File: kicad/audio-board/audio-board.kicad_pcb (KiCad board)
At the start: 4 copper layers, 70 x 50 mm, 120 parts, among them J1 AERONODE_FFC (mates J9), J3 CUP_L (A2B + speaker), J4 CUP_R (speaker), J5 PANEL (ear + mic), J6 FAILSAFE_ELECTRET, Q1 AO3401A, Q2 2N7002, T2 Triad SP-74 (cup L), T3 Triad SP-74 (cup R), T4 Bourns SM-LP-5001 (600:600), U1 TPS62162DSG, U10 AQW612S (K1 mic-hi), U11 AQW612S (K1 mic-lo), U12 LM2731XMF (8 V A2B bus), U2 TPS62160DSG, U3 ADP7118AUJZ-3.3-R7, U4 ADAU1467, U5 W25Q32JVSS, U6 ADAU1372, U7 IM68A130A, U9 AD2428WBCPZ, Y1 SiT8008 12.288MHz 3.3V

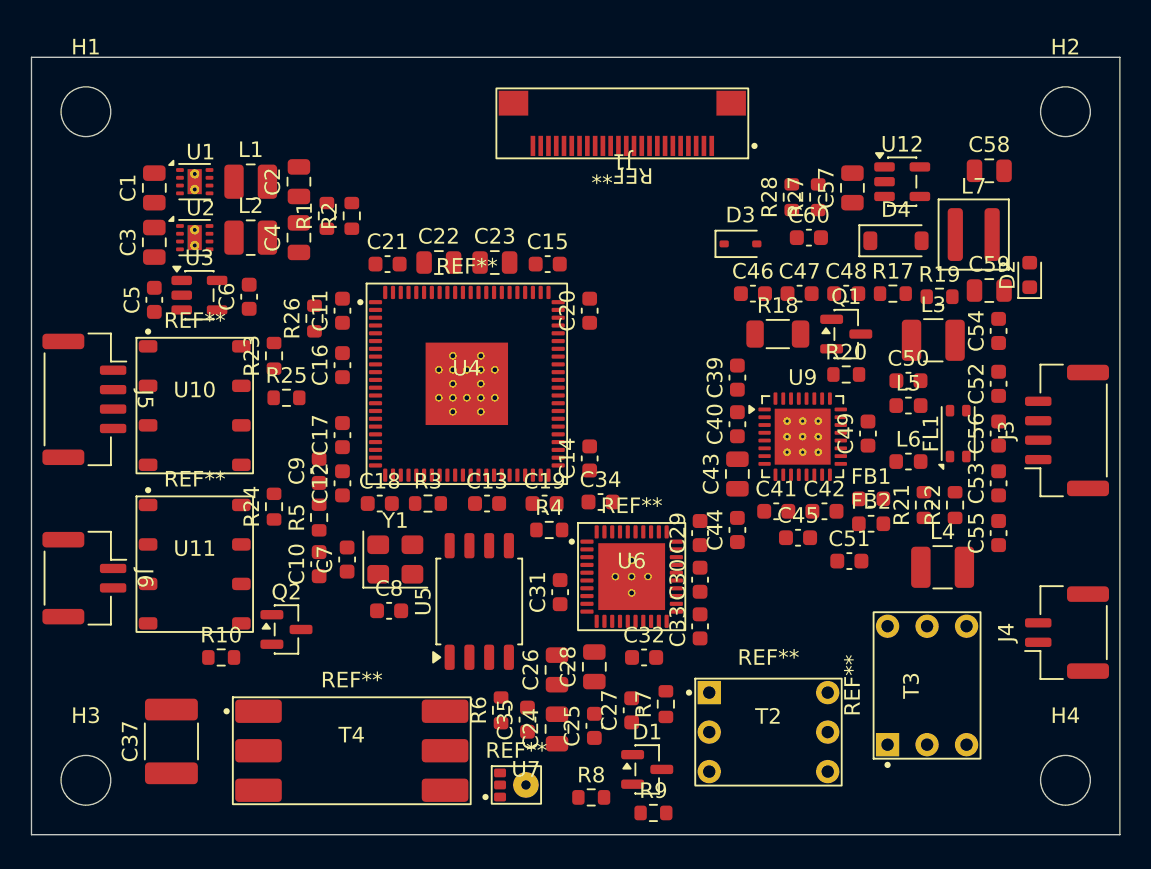
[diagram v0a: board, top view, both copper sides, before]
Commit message: [LIMA] audio PCB: GND/+3V3 plane fanout (126 pad vias + 21 EP vias), DRC 0
Scripted (doc/route/fanout.py, pcbnew, KiCad closed) - last autoroute stalled on plane fanout.

Co-Authored-By: Claude Opus 5.5 <noreply@anthropic.com>
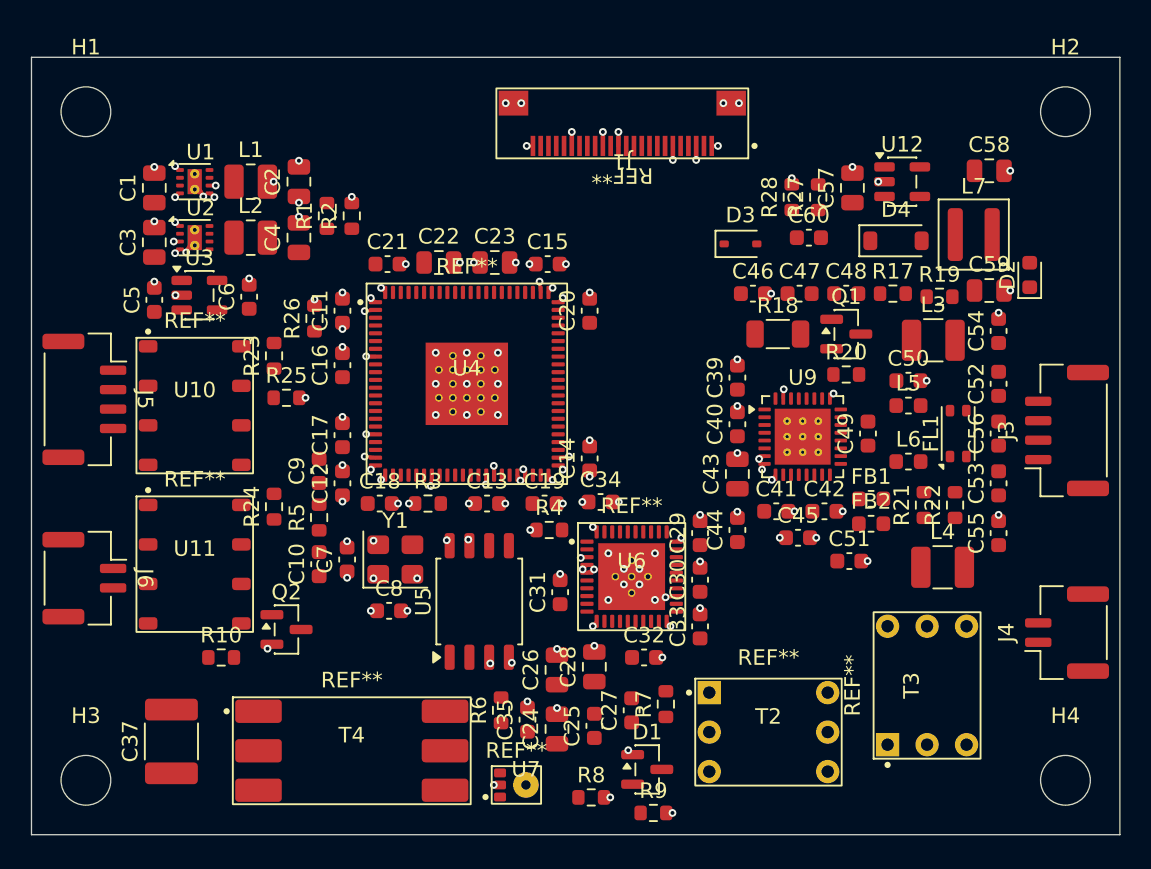
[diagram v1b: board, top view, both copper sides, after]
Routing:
- net /GND: track 0.00 -> 44.9 mm, vias 0 -> 119
- net /+3V3: track 0.00 -> 12.3 mm, vias 0 -> 28

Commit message: [LIMA] audio PCB: Freerouting pass (WIP) - 19 pads unconnected, 0 clearance errors
In1 GND / In2 +3V3 planes kept solid; VBAT/+3V3A routed 0.2 mm (fine-pitch pins), other power 0.3 mm.
Left: A2B I2S lines U4<->U9, some +3V3A/A2B_VIN links, 5 neckdowns <0.127 mm.

Co-Authored-By: Claude Opus 5.5 <noreply@anthropic.com>
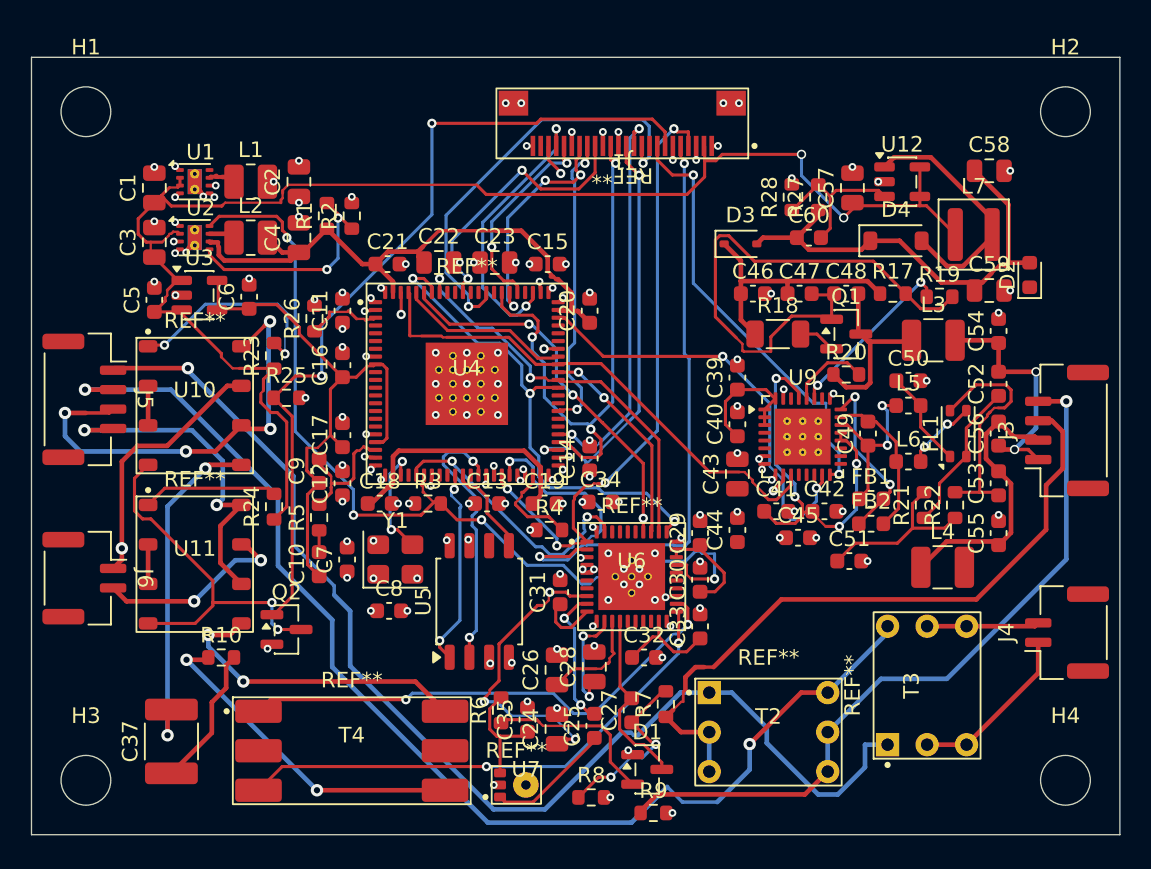
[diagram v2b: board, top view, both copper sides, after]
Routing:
- net /VBAT: track 0.00 -> 96.8 mm, vias 0 -> 2
- net /EAR_RTN: track 0.00 -> 76.6 mm, vias 0 -> 2
- net /EAR_HI: track 0.00 -> 75.5 mm, vias 0 -> 1
- net /RESET_N: track 0.00 -> 60.4 mm, vias 0 -> 4
- net /+3V3A: track 0.00 -> 58.9 mm
- net /+1V2: track 0.00 -> 54.8 mm
- net /CTL_MIC: track 0.00 -> 54.3 mm, vias 0 -> 2
- net /I2C_SCL: track 0.00 -> 50.6 mm, vias 0 -> 3
- net /SPK_L_B: track 0.00 -> 47.7 mm, vias 0 -> 1
- net /SPK_L_A: track 0.00 -> 44.6 mm
- net /I2C_SDA: track 0.00 -> 40.2 mm, vias 0 -> 4
- net /I2S_BCLK: track 0.00 -> 36.9 mm, vias 0 -> 3
- net /A2B_GATE: track 0.00 -> 35.8 mm
- net /DAC_N: track 0.00 -> 33.4 mm, vias 0 -> 2
- net /A2B_SYNC: track 0.00 -> 32.9 mm
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
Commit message: [LIMA] audio PCB: placement rev2 - boost cell tightened, U9 rotated to face hub (unrouted)
Back to the unrouted 3ab5285 board. L7 turned 180 so SW pad meets D4 anode; U12 r180 above L7
(SW node pads now ~2-3 mm apart, was 16 mm routed); C57/C59 at U12 VBAT / D4 cathode.
U9 r-90, 2 mm left: TDM pins 9-16 face U4; its 7 decaps re-placed at their pins; FB1/FB2 +0.4 mm.
DRC 0 violations. T2/T3 not moved (pending Peter: moving them lengthens 4 SPK nets).
Routed WIP stays in history at c929354.

Co-Authored-By: Claude Opus 5.5 <noreply@anthropic.com>
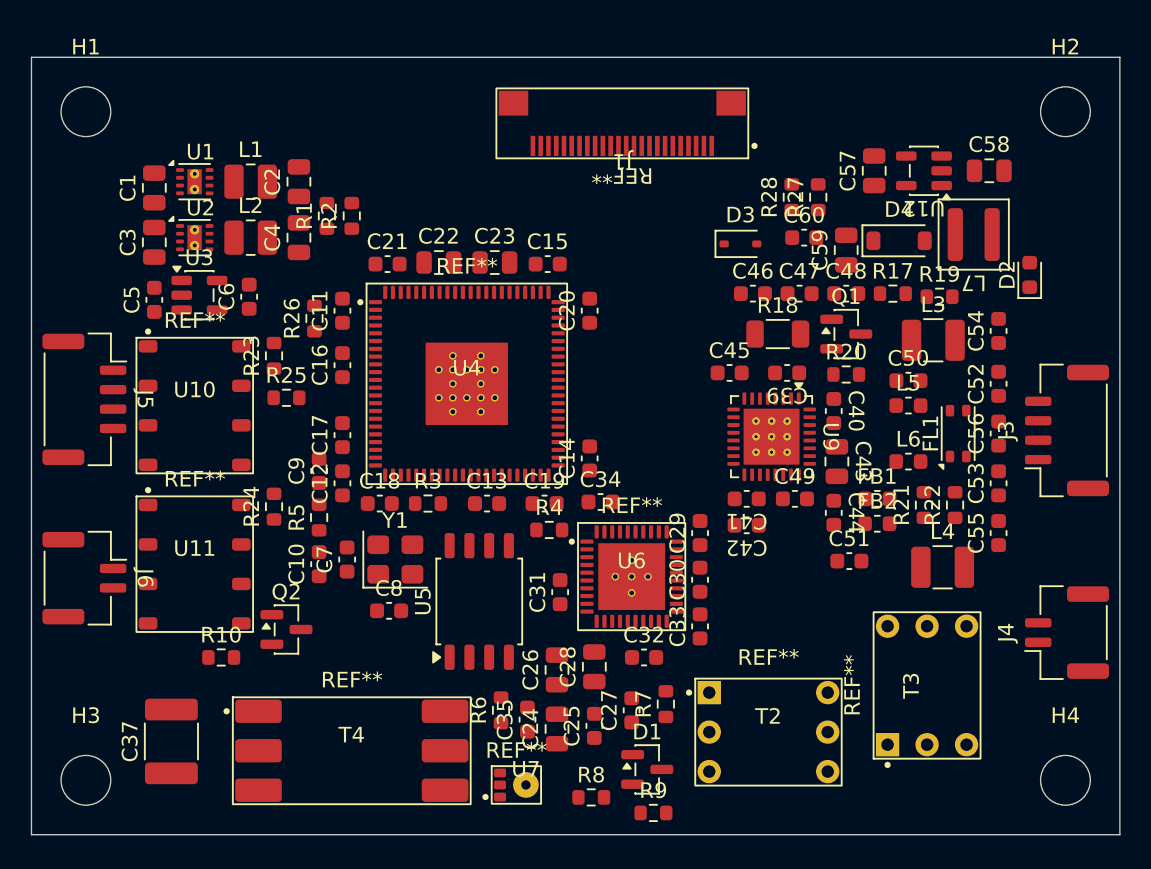
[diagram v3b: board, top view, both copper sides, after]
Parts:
- moved C45 11.5 mm to (144.9, 100.3)
- moved C59 9.56 mm to (152.4, 92.4), turned to 90 degrees
- moved C43 6.45 mm to (151.8, 106.0), turned to -90 degrees
- moved C49 6.30 mm to (149.1, 108.4), turned to 0 degrees
- moved C44 6.30 mm to (151.6, 109.3), turned to -90 degrees
- moved C40 6.26 mm to (151.6, 102.8), turned to -90 degrees
- moved C42 5.08 mm to (146.0, 110.1), turned to 180 degrees
- moved C39 3.21 mm to (148.6, 100.3), turned to 180 degrees
- moved C41 2.06 mm to (146.0, 108.4), turned to 180 degrees
- moved U9 2.00 mm to (147.6, 104.4), turned to -90 degrees
- moved C57 1.78 mm to (154.2, 87.3)
- moved U12 1.57 mm to (157.4, 87.3), turned to 180 degrees
- moved FB1 0.40 mm to (154.4, 108.4)
- moved FB2 0.40 mm to (154.4, 110.0)
- moved C60 0.30 mm to (149.7, 91.6)
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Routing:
- net /VBAT: track 96.8 -> 0.00 mm, vias 2 -> 0
- net /EAR_RTN: track 76.6 -> 0.00 mm, vias 2 -> 0
- net /EAR_HI: track 75.5 -> 0.00 mm, vias 1 -> 0
- net /RESET_N: track 60.4 -> 0.00 mm, vias 4 -> 0
- net /+3V3A: track 58.9 -> 0.00 mm
- net /+1V2: track 54.8 -> 0.00 mm
- net /CTL_MIC: track 54.3 -> 0.00 mm, vias 2 -> 0
- net /I2C_SCL: track 50.6 -> 0.00 mm, vias 3 -> 0
- net /SPK_L_B: track 47.7 -> 0.00 mm, vias 1 -> 0
- net /GND: track 44.9 -> 0.00 mm, vias 119 -> 0
- net /SPK_L_A: track 44.6 -> 0.00 mm
- net /I2C_SDA: track 40.2 -> 0.00 mm, vias 4 -> 0
- net /I2S_BCLK: track 36.9 -> 0.00 mm, vias 3 -> 0
- net /A2B_GATE: track 35.8 -> 0.00 mm
- net /DAC_N: track 33.4 -> 0.00 mm, vias 2 -> 0
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
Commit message: [LIMA] audio PCB: EAR corridor, isolation turns, hand routes, plane fanout (pre-autoroute)
- U10/U11/T4 turned 180: aircraft-side pins now face J5/J6 and the aircraft corner
  (U10 LED pins were 0.8 mm from J5's EAR pads); T4 DAC side now faces the codec.
- In1/In2 cut back under the EAR corridor, T2 and T3 (doc/route/planecut.py).
- Hand routes (locked, doc/route/hand-routes.json): EAR pair B.Cu bottom edge 0.3/0.55 gap,
  EAR_HI T2->T3 link on F.Cu; boost SW node 0.6/0.8 mm, D4->C59, C57->U12 VBAT; A2B LINE_P/N at J3.
- Plane fanout re-run, now aware of B.Cu tracks and the plane outline.
DRC: 0 violations, 196 unconnected (to autoroute).

Co-Authored-By: Claude Opus 5.5 <noreply@anthropic.com>
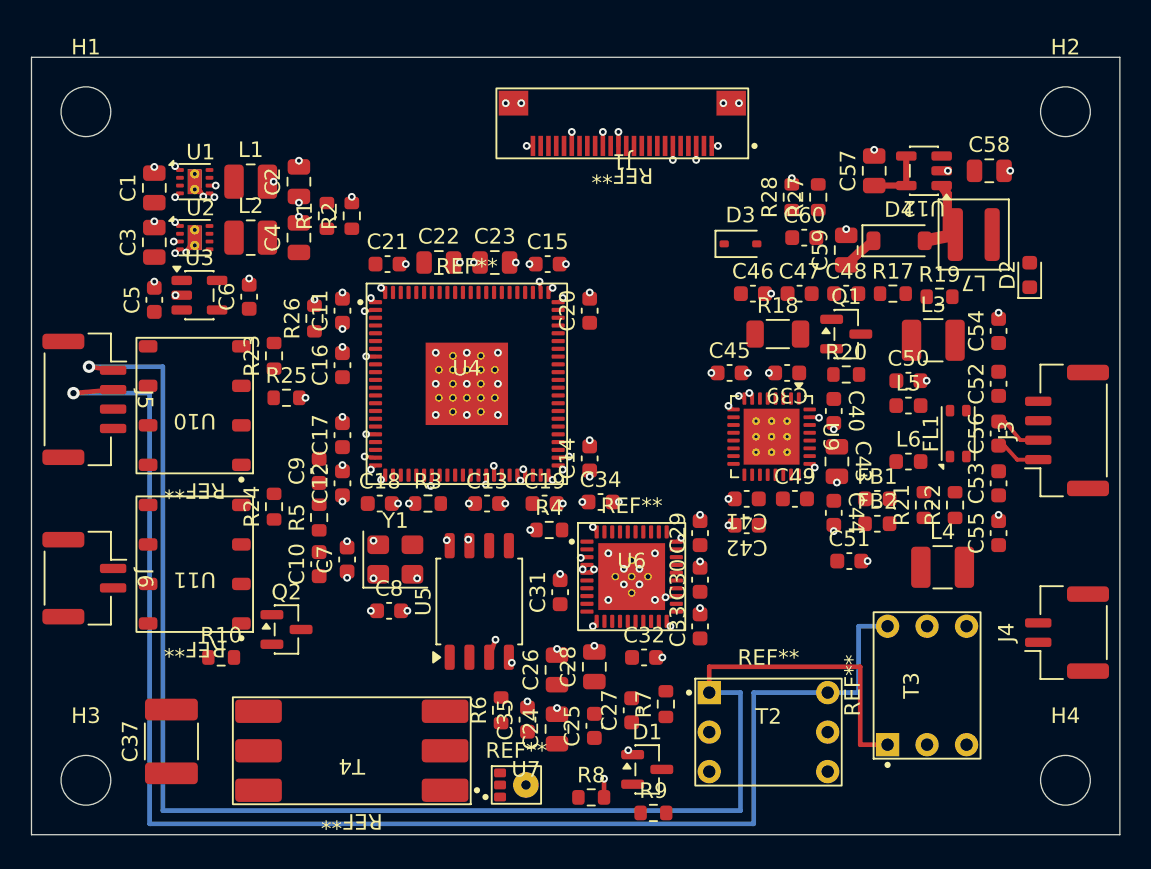
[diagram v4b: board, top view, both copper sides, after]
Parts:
- turned T4 to 180 degrees
- turned U10 to 180 degrees
- turned U11 to 180 degrees
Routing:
- net /EAR_HI: track 0.00 -> 99.8 mm, vias 0 -> 1
- net /EAR_RTN: track 0.00 -> 95.3 mm, vias 0 -> 1
- net /GND: track 0.00 -> 44.5 mm, vias 0 -> 116
- net /+3V3: track 0.00 -> 13.1 mm, vias 0 -> 28
- net /BOOST_SW: track 0.00 -> 5.77 mm
- net /VBAT: track 0.00 -> 3.96 mm
- net /A2B_LINE_N: track 0.00 -> 3.11 mm
- net /A2B_LINE_P: track 0.00 -> 2.94 mm
- net /VBUS8: track 0.00 -> 2.34 mm

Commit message: [LIMA] audio PCB: autoroute on the corridor build - 18 unconnected, 0 clearance errors (WIP)
Scripted pipeline doc/route/build.sh (rev2 placement -> isolation turns -> U9 cap column moved out
-> plane cut -> hand routes -> fanout -> DSN). Freerouting best variant: In2 kept a solid plane,
0.13 mm clearance, 0.5/0.25 vias. SES import + tolerant de-dupe (pcbnew segfault workarounds).

Co-Authored-By: Claude Opus 5.5 <noreply@anthropic.com>
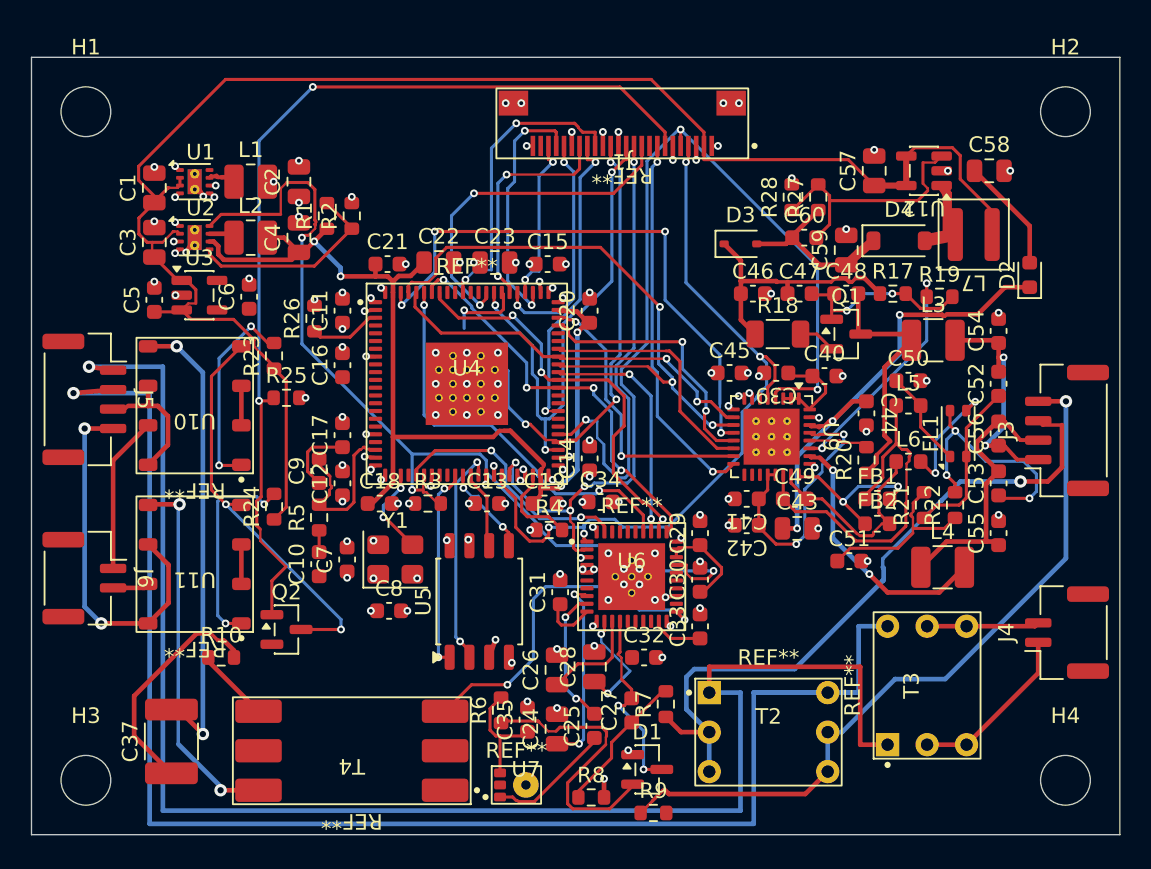
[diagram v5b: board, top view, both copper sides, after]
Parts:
- moved C44 6.74 mm to (153.7, 102.9)
- moved R20 5.65 mm to (153.7, 105.9), turned to 90 degrees
- moved C43 5.00 mm to (149.2, 110.3), turned to 0 degrees
- moved C40 2.33 mm to (151.0, 100.5), turned to 0 degrees
- moved C39 0.70 mm to (147.9, 100.3)
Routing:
- net /VBAT: track 3.96 -> 104.7 mm
- net /+1V2: track 0.00 -> 65.0 mm, vias 0 -> 4
- net /I2C_SCL: track 0.00 -> 64.7 mm, vias 0 -> 5
- net /CTL_MIC: track 0.00 -> 62.4 mm, vias 0 -> 2
- net /RESET_N: track 0.00 -> 61.8 mm, vias 0 -> 3
- net /I2C_SDA: track 0.00 -> 49.0 mm, vias 0 -> 4
- net /SPK_L_B: track 0.00 -> 47.7 mm, vias 0 -> 1
- net /SPK_L_A: track 0.00 -> 44.9 mm, vias 0 -> 1
- net /A2B_SYNC: track 0.00 -> 38.2 mm, vias 0 -> 3
- net /A2B_DTX0: track 0.00 -> 36.6 mm, vias 0 -> 4
- net /I2S_BCLK: track 0.00 -> 35.2 mm, vias 0 -> 4
- net /I2S_WS: track 0.00 -> 32.6 mm, vias 0 -> 3
- net /A2B_VIN: track 0.00 -> 31.0 mm, vias 0 -> 3
- net /PV_OUT: track 0.00 -> 30.2 mm, vias 0 -> 2
- net /HOST_SDI0: track 0.00 -> 29.8 mm, vias 0 -> 2
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
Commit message: [LIMA] audio PCB: fully routed - 0 unconnected, 0 DRC errors
Freerouting left 18; finished with doc/route/maze.py (A* on F.Cu/B.Cu over the real copper,
clearance-inflated) - 16/18 at 0.2 mm, then C33 moved +0.8 mm to open U6's DAC corner, DAC pair
ripped and re-routed with C33's links. Shadow duplicates from SES import removed.
Hand-check [measured]: BOOST_SW 5.8 mm (was 16); EAR_HI/RTN 99.8/95.3 mm, pair over no plane;
all EAR/MIC/ELEC/PV copper over no plane; SPK (isolated secondaries) cross planes.
DRC remaining: silk warnings, 116 lib_footprint_mismatch (known), 5 datasheet-field parity warnings.

Co-Authored-By: Claude Opus 5.5 <noreply@anthropic.com>
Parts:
- moved C33 0.80 mm to (143.8, 116.6)
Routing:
- net /+3V3A: track 29.5 -> 88.1 mm, vias 0 -> 12
- net /GND: track 44.5 -> 82.3 mm
- net /DAC_P: track 0.00 -> 25.8 mm, vias 0 -> 2
- net /VBUS8: track 18.8 -> 28.2 mm
- net /EAR_RTN: track 102.1 -> 95.3 mm
- net /DAC_N: track 22.6 -> 17.2 mm
- net /I2S_BCLK: track 35.2 -> 37.7 mm
- net /CODEC_BCLK: vias 3 -> 2

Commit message: [LIMA] audio PCB: J3 -> 6-pin, J4 -> 4-pin GH, boom electret routed to J6/K1 - 0 unconnected, 0 errors
J3/J4 seated so their old pins land where they were (A2B + speaker routes kept). ELEC_HI/LO J3<->J4 links
hand-routed down the right edge under the connector bodies (doc/route/elec-links.json, locked), ELEC to J6 by
maze at Aircraft clearance (top-edge path). SPK_L_A/B restored from the committed board, re-joined near J3.
Parity: only the 5 old field-mismatch warnings. READMEs: pass-through, J12 pads, cup R split harness.
copynet.py: copy a net's copper from one board to another (restore a displaced route).

Co-Authored-By: Claude Opus 5.5 <noreply@anthropic.com>
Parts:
- J3: value CUP_L (A2B + speaker) -> CUP_L (A2B + speaker + boom electret); footprint Connector_JST:JST_GH_SM04B-GHS-TB_1x04-1MP_P1.25mm_Horizontal -> Connector_JST:JST_GH_SM06B-GHS-TB_1x06-1MP_P1.25mm_Horizontal
- J4: value CUP_R (speaker) -> CUP_R (speaker + boom electret); footprint Connector_JST:JST_GH_SM02B-GHS-TB_1x02-1MP_P1.25mm_Horizontal -> Connector_JST:JST_GH_SM04B-GHS-TB_1x04-1MP_P1.25mm_Horizontal
- moved J4 1.25 mm to (166.6, 115.8)
- moved J3 1.25 mm to (166.6, 102.8)
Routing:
- net /ELEC_LO: track 2.36 -> 117.8 mm, vias 0 -> 3
- net /ELEC_HI: track 10.1 -> 110.7 mm, vias 0 -> 6
- net /SPK_L_B: track 47.7 -> 52.4 mm, vias 1 -> 2
